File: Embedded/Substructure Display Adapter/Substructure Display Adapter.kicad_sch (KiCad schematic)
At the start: 18 parts, among them J1 HUB75, J2 Input, J3 Output, J4 HUB75, J5 Input, J6 Output, U1 D0 FFC, U2 74HC245D_653, U3 74HC245D_653, U4 D0 FFC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

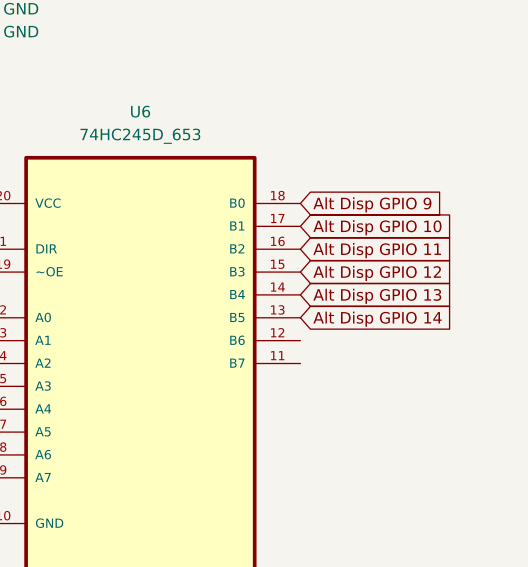
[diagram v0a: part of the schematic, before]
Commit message: Added Routing for right adapter
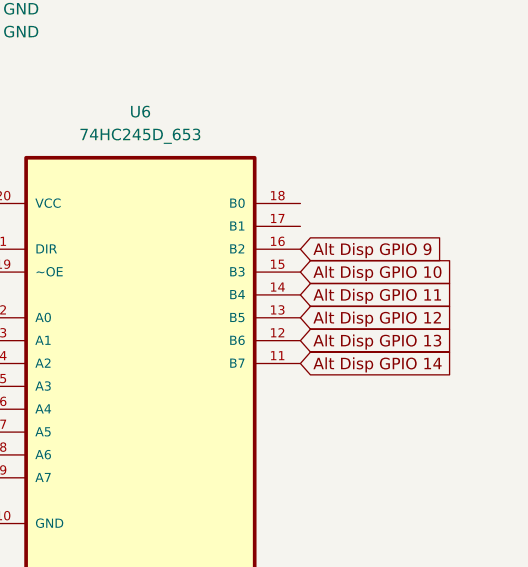
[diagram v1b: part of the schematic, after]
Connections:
- net Alt Disp GPIO 10: now also U6.15 (B3); no longer U6.17 (B1)
- net Alt Disp GPIO 11: now also U6.14 (B4); no longer U6.16 (B2)
- net Alt Disp GPIO 12: now also U6.13 (B5); no longer U6.15 (B3)
- net Alt Disp GPIO 13: now also U6.12 (B6); no longer U6.14 (B4)
- net Alt Disp GPIO 14: now also U6.11 (B7); no longer U6.13 (B5)
- net Alt Disp GPIO 9: now also U6.16 (B2); no longer U6.18 (B0)

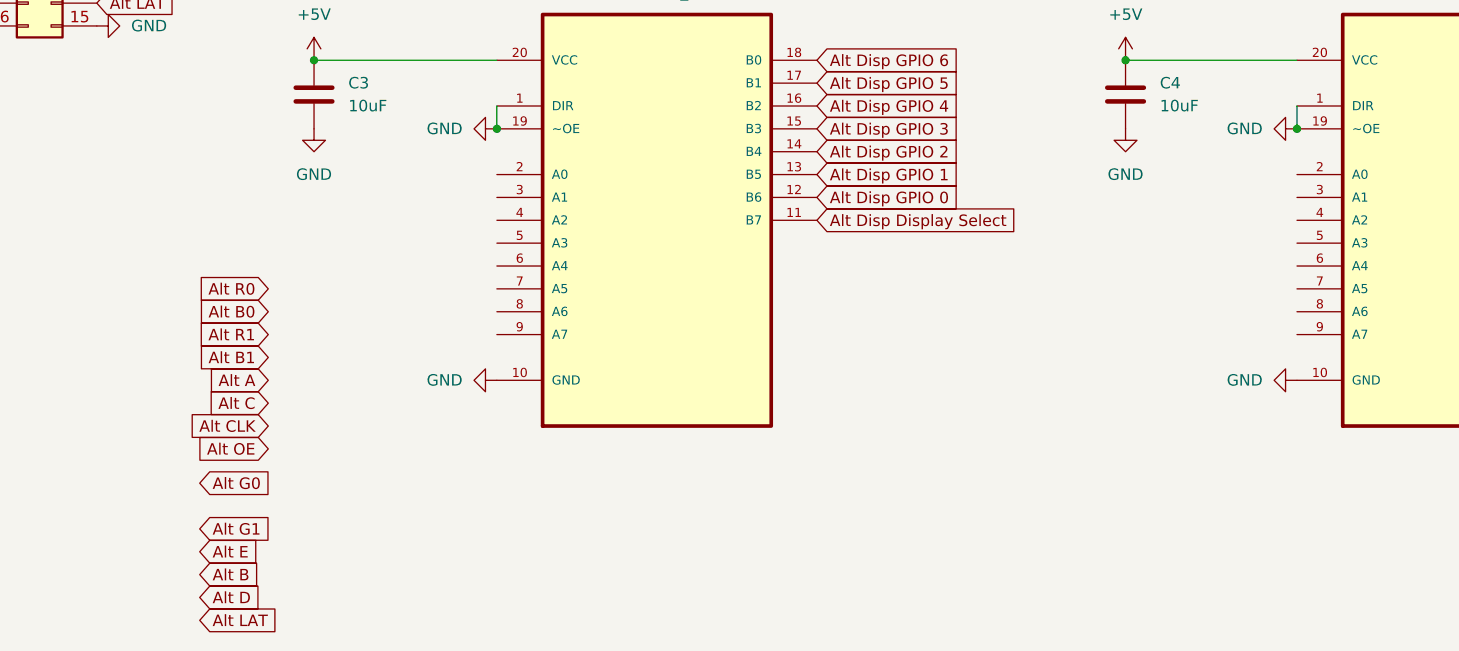
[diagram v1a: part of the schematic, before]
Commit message: Added Routing for left adapter
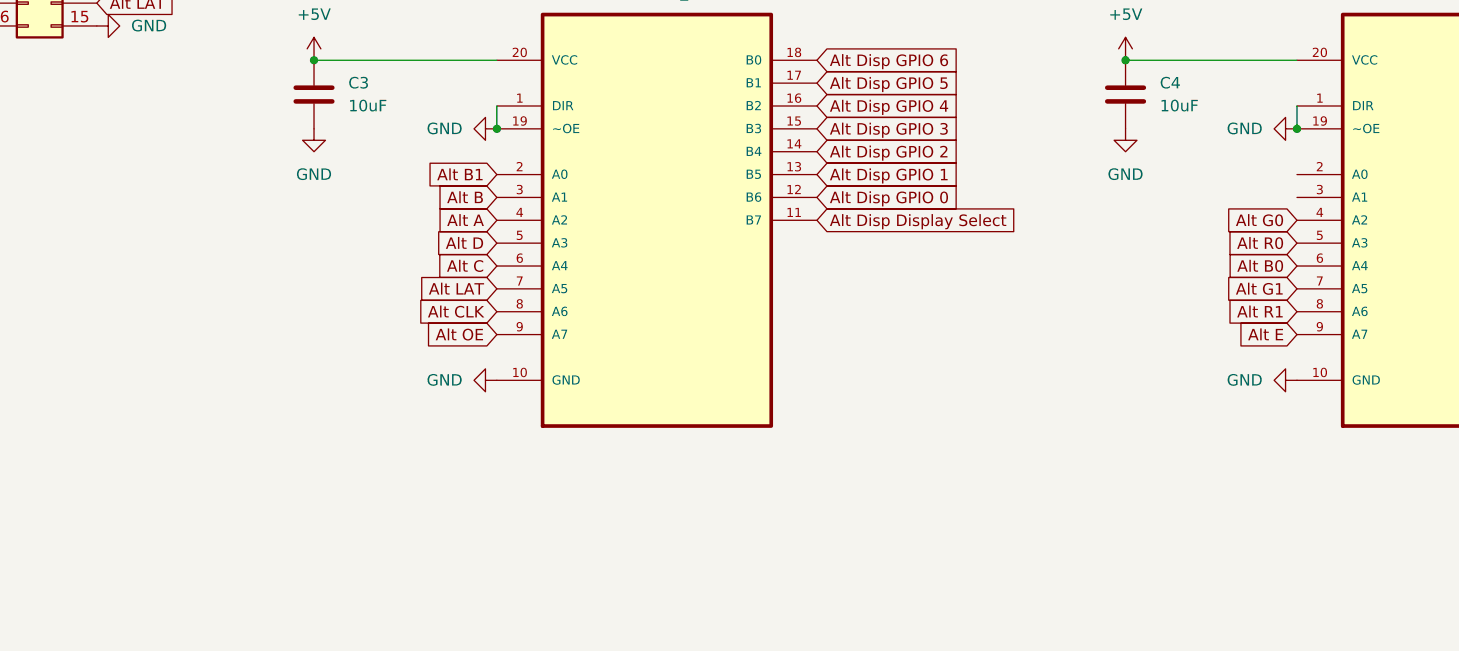
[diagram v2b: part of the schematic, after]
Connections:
- net Alt A: now also U5.4 (A2)
- net Alt B: now also U5.3 (A1)
- net Alt B0: now also U6.6 (A4)
- net Alt B1: now also U5.2 (A0)
- net Alt C: now also U5.6 (A4)
- net Alt CLK: now also U5.8 (A6)
- net Alt D: now also U5.5 (A3)
- net Alt E: now also U6.9 (A7)
- net Alt G0: now also U6.4 (A2)
- net Alt G1: now also U6.7 (A5)
- net Alt LAT: now also U5.7 (A5)
- net Alt OE: now also U5.9 (A7)
- net Alt R0: now also U6.5 (A3)
- net Alt R1: now also U6.8 (A6)
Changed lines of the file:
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@@
 	(global_label "Alt R1"
 		(shape input)
-		(at 100.33 153.67 180)
-		(fields_autoplaced yes)
-		(effects
-			(font
-				(size 1.27 1.27)
-			)
-			(justify right)
-		)
-		(property "Intersheetrefs" "${INTERSHEET_REFS}"
-			(at 91.4182 153.67 0)
+		(at 214.63 151.13 180)
+		(fields_autoplaced yes)
+		(effects
+			(font
+				(size 1.27 1.27)
+			)
+			(justify right)
+		)
+		(property "Intersheetrefs" "${INTERSHEET_REFS}"
+			(at 205.7182 151.13 0)
 			(effects
 				(font
@@
 	(global_label "Alt G0"
 		(shape input)
-		(at 92.71 170.18 0)
-		(fields_autoplaced yes)
-		(effects
-			(font
-				(size 1.27 1.27)
-			)
-			(justify left)
-		)
-		(property "Intersheetrefs" "${INTERSHEET_REFS}"
-			(at 101.6218 170.18 0)
-			(effects
-				(font
-					(size 1.27 1.27)
-				)
-				(justify left)
+		(at 214.63 140.97 180)
+		(fields_autoplaced yes)
+		(effects
+			(font
+				(size 1.27 1.27)
+			)
+			(justify right)
+		)
+		(property "Intersheetrefs" "${INTERSHEET_REFS}"
+			(at 205.7182 140.97 0)
+			(effects
+				(font
+					(size 1.27 1.27)
+				)
+				(justify right)
 				(hide yes)
 			)
@@
 	(global_label "Alt CLK"
 		(shape input)
-		(at 100.33 163.83 180)
-		(fields_autoplaced yes)
-		(effects
-			(font
-				(size 1.27 1.27)
-			)
-			(justify right)
-		)
-		(property "Intersheetrefs" "${INTERSHEET_REFS}"
-			(at 90.3296 163.83 0)
+		(at 125.73 151.13 180)
+		(fields_autoplaced yes)
+		(effects
+			(font
+				(size 1.27 1.27)
+			)
+			(justify right)
+		)
+		(property "Intersheetrefs" "${INTERSHEET_REFS}"
+			(at 115.7296 151.13 0)
 			(effects
 				(font
@@
 	(global_label "Alt G1"
 		(shape input)
-		(at 92.71 175.26 0)
-		(fields_autoplaced yes)
-		(effects
-			(font
-				(size 1.27 1.27)
-			)
-			(justify left)
-		)
-		(property "Intersheetrefs" "${INTERSHEET_REFS}"
-			(at 101.6218 175.26 0)
-			(effects
-				(font
-					(size 1.27 1.27)
-				)
-				(justify left)
+		(at 214.63 148.59 180)
+		(fields_autoplaced yes)
+		(effects
+			(font
+				(size 1.27 1.27)
+			)
+			(justify right)
+		)
+		(property "Intersheetrefs" "${INTERSHEET_REFS}"
+			(at 205.7182 148.59 0)
+			(effects
+				(font
+					(size 1.27 1.27)
+				)
+				(justify right)
 				(hide yes)
 			)
@@
 	(global_label "Alt B0"
 		(shape input)
-		(at 100.33 151.13 180)
-		(fields_autoplaced yes)
-		(effects
-			(font
-				(size 1.27 1.27)
-			)
-			(justify right)
-		)
-		(property "Intersheetrefs" "${INTERSHEET_REFS}"
-			(at 91.4182 151.13 0)
+		(at 214.63 146.05 180)
+		(fields_autoplaced yes)
+		(effects
+			(font
+				(size 1.27 1.27)
+			)
+			(justify right)
+		)
+		(property "Intersheetrefs" "${INTERSHEET_REFS}"
+			(at 205.7182 146.05 0)
 			(effects
 				(font
@@
 	(global_label "Alt C"
 		(shape input)
-		(at 100.33 161.29 180)
-		(fields_autoplaced yes)
-		(effects
-			(font
-				(size 1.27 1.27)
-			)
-			(justify right)
-		)
-		(property "Intersheetrefs" "${INTERSHEET_REFS}"
-			(at 92.6277 161.29 0)
+		(at 125.73 146.05 180)
+		(fields_autoplaced yes)
+		(effects
+			(font
+				(size 1.27 1.27)
+			)
+			(justify right)
+		)
+		(property "Intersheetrefs" "${INTERSHEET_REFS}"
+			(at 118.0277 146.05 0)
 			(effects
 				(font
@@
 	(global_label "Alt E"
 		(shape input)
-		(at 92.71 177.8 0)
-		(fields_autoplaced yes)
-		(effects
-			(font
-				(size 1.27 1.27)
-			)
-			(justify left)
-		)
-		(property "Intersheetrefs" "${INTERSHEET_REFS}"
-			(at 100.2913 177.8 0)
-			(effects
-				(font
-					(size 1.27 1.27)
-				)
-				(justify left)
+		(at 214.63 153.67 180)
+		(fields_autoplaced yes)
+		(effects
+			(font
+				(size 1.27 1.27)
+			)
+			(justify right)
+		)
+		(property "Intersheetrefs" "${INTERSHEET_REFS}"
+			(at 207.0487 153.67 0)
+			(effects
+				(font
+					(size 1.27 1.27)
+				)
+				(justify right)
 				(hide yes)
 			)
@@
 	(global_label "Alt B"
 		(shape input)
-		(at 92.71 180.34 0)
-		(fields_autoplaced yes)
-		(effects
-			(font
-				(size 1.27 1.27)
-			)
-			(justify left)
-		)
-		(property "Intersheetrefs" "${INTERSHEET_REFS}"
-			(at 100.4123 180.34 0)
-			(effects
-				(font
-					(size 1.27 1.27)
-				)
-				(justify left)
+		(at 125.73 138.43 180)
+		(fields_autoplaced yes)
+		(effects
+			(font
+				(size 1.27 1.27)
+			)
+			(justify right)
+		)
+		(property "Intersheetrefs" "${INTERSHEET_REFS}"
+			(at 118.0277 138.43 0)
+			(effects
+				(font
+					(size 1.27 1.27)
+				)
+				(justify right)
 				(hide yes)
 			)
@@
 	(global_label "Alt D"
 		(shape input)
-		(at 92.71 182.88 0)
-		(fields_autoplaced yes)
-		(effects
-			(font
-				(size 1.27 1.27)
-			)
-			(justify left)
-		)
-		(property "Intersheetrefs" "${INTERSHEET_REFS}"
-			(at 100.4123 182.88 0)
-			(effects
-				(font
-					(size 1.27 1.27)
-				)
-				(justify left)
+		(at 125.73 143.51 180)
+		(fields_autoplaced yes)
+		(effects
+			(font
+				(size 1.27 1.27)
+			)
+			(justify right)
+		)
+		(property "Intersheetrefs" "${INTERSHEET_REFS}"
+			(at 118.0277 143.51 0)
+			(effects
+				(font
+					(size 1.27 1.27)
+				)
+				(justify right)
 				(hide yes)
 			)
@@
 	(global_label "Alt R0"
 		(shape input)
-		(at 100.33 148.59 180)
-		(fields_autoplaced yes)
-		(effects
-			(font
-				(size 1.27 1.27)
-			)
-			(justify right)
-		)
-		(property "Intersheetrefs" "${INTERSHEET_REFS}"
-			(at 91.4182 148.59 0)
+		(at 214.63 143.51 180)
+		(fields_autoplaced yes)
+		(effects
+			(font
+				(size 1.27 1.27)
+			)
+			(justify right)
+		)
+		(property "Intersheetrefs" "${INTERSHEET_REFS}"
+			(at 205.7182 143.51 0)
 			(effects
 				(font
@@
 	(global_label "Alt LAT"
 		(shape input)
-		(at 92.71 185.42 0)
-		(fields_autoplaced yes)
-		(effects
-			(font
-				(size 1.27 1.27)
-			)
-			(justify left)
-		)
-		(property "Intersheetrefs" "${INTERSHEET_REFS}"
-			(at 102.2266 185.42 0)
-			(effects
-				(font
-					(size 1.27 1.27)
-				)
-				(justify left)
+		(at 125.73 148.59 180)
+		(fields_autoplaced yes)
+		(effects
+			(font
+				(size 1.27 1.27)
+			)
+			(justify right)
+		)
+		(property "Intersheetrefs" "${INTERSHEET_REFS}"
+			(at 116.2134 148.59 0)
+			(effects
+				(font
+					(size 1.27 1.27)
+				)
+				(justify right)
 				(hide yes)
 			)
@@
 	(global_label "Alt B1"
 		(shape input)
-		(at 100.33 156.21 180)
-		(fields_autoplaced yes)
-		(effects
-			(font
-				(size 1.27 1.27)
-			)
-			(justify right)
-		)
-		(property "Intersheetrefs" "${INTERSHEET_REFS}"
-			(at 91.4182 156.21 0)
+		(at 125.73 135.89 180)
+		(fields_autoplaced yes)
+		(effects
+			(font
+				(size 1.27 1.27)
+			)
+			(justify right)
+		)
+		(property "Intersheetrefs" "${INTERSHEET_REFS}"
+			(at 116.8182 135.89 0)
 			(effects
 				(font
@@
 	(global_label "Alt OE"
 		(shape input)
-		(at 100.33 166.37 180)
-		(fields_autoplaced yes)
-		(effects
-			(font
-				(size 1.27 1.27)
-			)
-			(justify right)
-		)
-		(property "Intersheetrefs" "${INTERSHEET_REFS}"
-			(at 91.4182 166.37 0)
+		(at 125.73 153.67 180)
+		(fields_autoplaced yes)
+		(effects
+			(font
+				(size 1.27 1.27)
+			)
+			(justify right)
+		)
+		(property "Intersheetrefs" "${INTERSHEET_REFS}"
+			(at 116.8182 153.67 0)
 			(effects
 				(font
@@
 	(global_label "Alt A"
 		(shape input)
-		(at 100.33 158.75 180)
-		(fields_autoplaced yes)
-		(effects
-			(font
-				(size 1.27 1.27)
-			)
-			(justify right)
-		)
-		(property "Intersheetrefs" "${INTERSHEET_REFS}"
-			(at 92.8091 158.75 0)
-			(effects
-				(font
+		(at 125.73 140.97 180)
+		(fields_autoplaced yes)
+		(effects
+			(font
+				(size 1.27 1.27)
+			)
+			(justify right)
+		)
+		(property "Intersheetrefs" "${INTERSHEET_REFS}"
+			(at 118.2091 140.97 0)
+			(effects
+				(font
